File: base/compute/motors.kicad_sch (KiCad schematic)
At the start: 18 parts, among them U4 W25X20CLSN, U5 ICE40UP5K-SG48ITR-FPGA_Lattice

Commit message: compute  module ready for fab
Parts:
- U5: footprint Package_DFN_QFN:QFN-48-1EP_7x7mm_P0.5mm_EP5.6x5.6mm -> footprints:QFN-48-1EP_7x7mm_P0.5mm_EP5.6x5.6mm
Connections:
- net FPGA36 is gone; now on net SPI_SS_FPGA: U5.25 (IOT_36b)
- net FPGA37 is gone; now on net Z_PO: U5.23 (IOT_37a)
- net FPGA48 is gone; now on net DIGITAL: U5.36 (IOT_48b)
- net FPGA50 is gone; now on net HALL2: U5.38 (IOT_50b)
- net FPGA51 is gone; now on net HALL3: U5.42 (IOT_51a)
- net DIGITAL: no longer U5.31 (IOT_42b)
- net HALL1: now also U5.37 (IOT_45a_G1); no longer U5.34 (IOT_44b)
- net HALL2: no longer U5.32 (IOT_43a)
- net HALL3: no longer U5.37 (IOT_45a_G1)
- net SPI_SS_FPGA: no longer U5.10 (IOB_18a)
- net Y_DIR: now also U5.10 (IOB_18a); no longer U5.21 (IOB_23b)
- net Y_PO: now also U5.12 (IOB_22a); no longer U5.11 (IOB_20a)
- net Y_STEP: now also U5.11 (IOB_20a); no longer U5.12 (IOB_22a)
- net Z_DIR: now also U5.20 (IOB_25b_G3); no longer U5.28 (IOT_41a)
- net Z_PO: no longer U5.20 (IOB_25b_G3)
- net Z_STEP: now also U5.21 (IOB_23b); no longer U5.27 (IOT_38b)
- net +3V3 renamed +3.3V
- net FREE renamed FPGA39
- new net FPGA38: U5.27 (IOT_38b)
- new net FPGA41: U5.28 (IOT_41a)
- new net FPGA42: U5.31 (IOT_42b)
- new net FPGA43: U5.32 (IOT_43a)
- new net FPGA44: U5.34 (IOT_44b)
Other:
- note added: "SPI wires doubled, not sure on SPI on ultraplus https://github.com/YosysHQ/icestorm/issues/174"

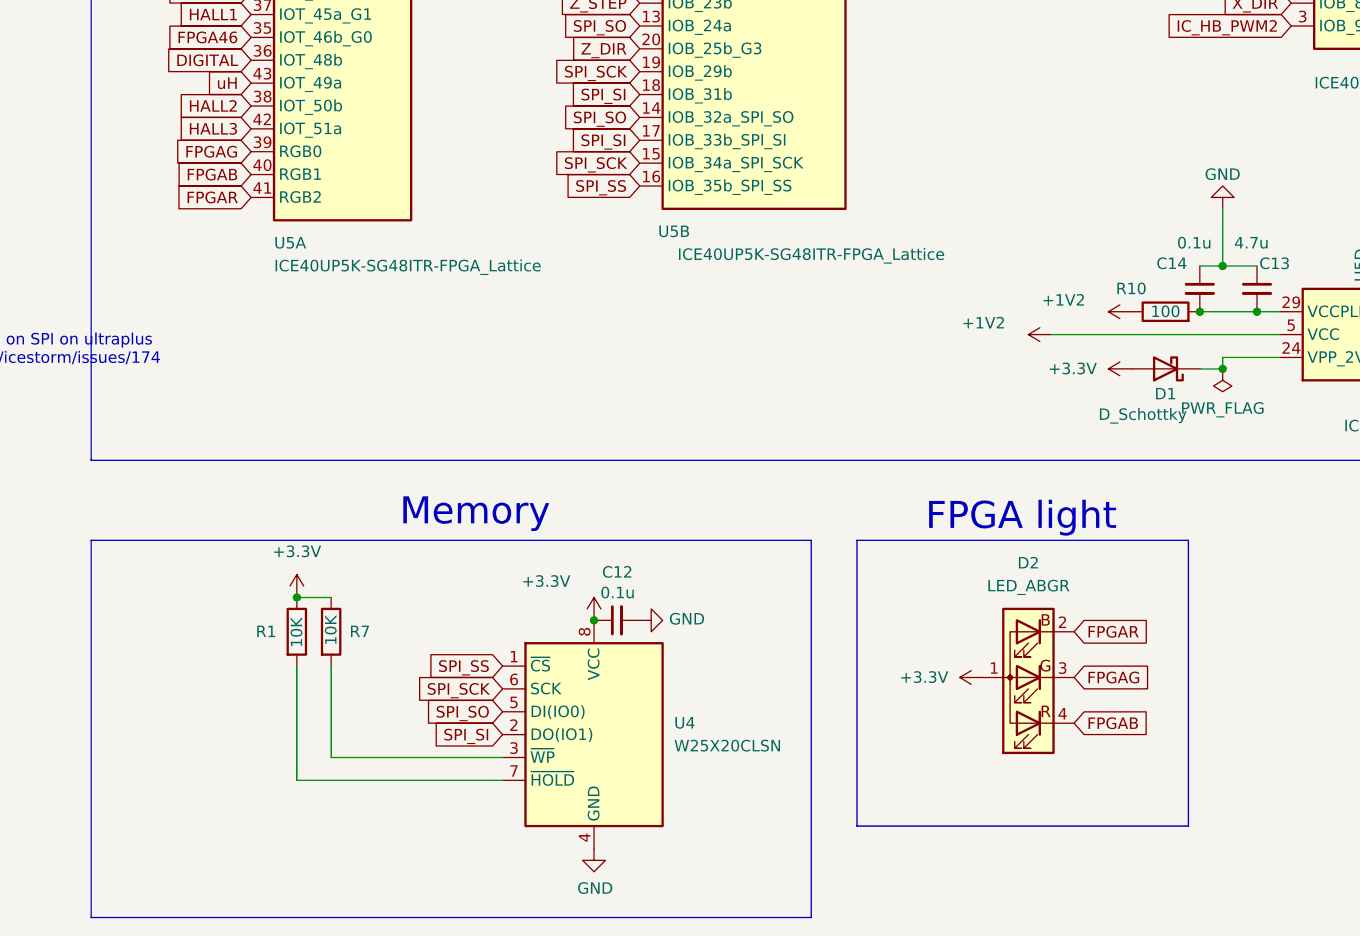
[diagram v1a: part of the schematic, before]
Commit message: moved from 2 headers to 1 smt 40 pin header
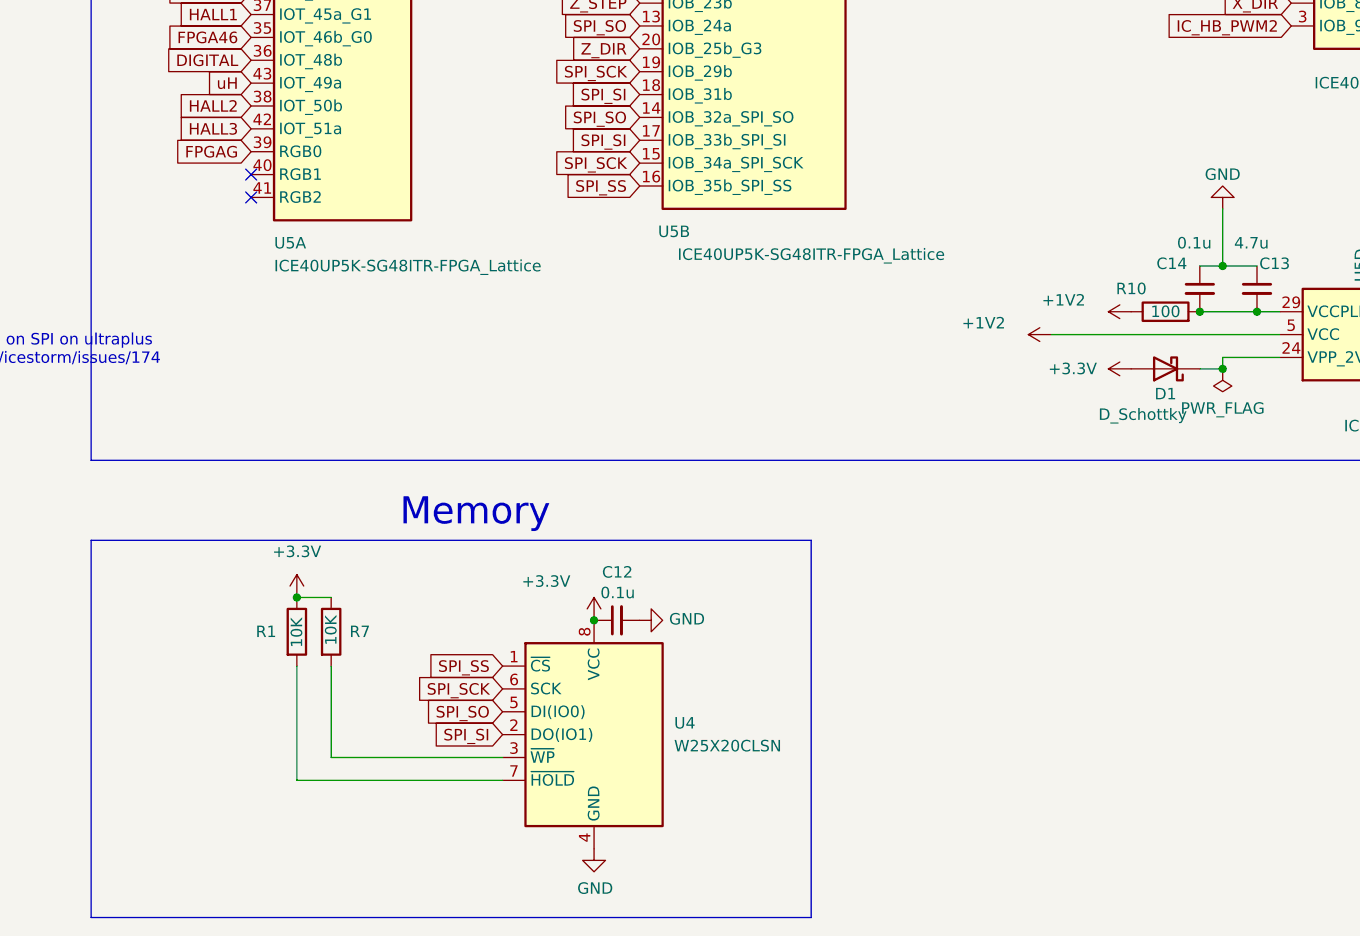
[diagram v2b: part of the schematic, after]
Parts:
- removed D2: LED_ABGR, footprints:LED_Cree-PLCC4_2x2mm_CW, symbol Device:LED_ABGR
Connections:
- net FPGAB: no longer names the net of U5.40 (RGB1)
- net FPGAR: no longer names the net of U5.41 (RGB2)
- no-connect marks 0 -> 2
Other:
- note removed: "FPGA light"

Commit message: retracking board
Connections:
- net FPGA38 is gone; now on net Z_DIR: U5.27 (IOT_38b)
- net FPGA39 is gone; now on net X_STEP: U5.26 (IOT_39a)
- net FPGA46 is gone; now on net Z_STEP: U5.35 (IOT_46b_G0)
- net DIGITAL: now also U5.46 (IOB_0a); no longer U5.36 (IOT_48b)
- net HALL1: now also U5.45 (IOB_5b); no longer U5.37 (IOT_45a_G1)
- net HALL2: now also U5.47 (IOB_2a); no longer U5.38 (IOT_50b)
- net HALL3: now also U5.48 (IOB_4a); no longer U5.42 (IOT_51a)
- net IC_HB_PWM1: now also U5.11 (IOB_20a); no longer U5.2 (IOB_6a)
- net IC_HB_PWM2: now also U5.12 (IOB_22a); no longer U5.3 (IOB_9b)
- net X_DIR: now also U5.20 (IOB_25b_G3); no longer U5.4 (IOB_8a)
- net X_PO: now also U5.42 (IOT_51a); no longer U5.9 (IOB_16a)
- net X_STEP: no longer U5.6 (IOB_13b)
- net Y_DIR: now also U5.36 (IOT_48b); no longer U5.10 (IOB_18a)
- net Y_PO: now also U5.21 (IOB_23b); no longer U5.12 (IOB_22a)
- net Y_STEP: now also U5.37 (IOT_45a_G1); no longer U5.11 (IOB_20a)
- net Z_DIR: no longer U5.20 (IOB_25b_G3)
- net Z_STEP: no longer U5.21 (IOB_23b)
- net uH: now also U5.4 (IOB_8a); no longer U5.43 (IOT_49a)
- net uL: now also U5.2 (IOB_6a); no longer U5.44 (IOB_3b_G6)
- net vH: now also U5.6 (IOB_13b); no longer U5.45 (IOB_5b)
- net vL: now also U5.3 (IOB_9b); no longer U5.46 (IOB_0a)
- net wH: now also U5.10 (IOB_18a); no longer U5.47 (IOB_2a)
- net wL: now also U5.9 (IOB_16a); no longer U5.48 (IOB_4a)
- net FPGA41 renamed INDEX_X
- new net FPGA3: U5.44 (IOB_3b_G6)
- new net FPGA49: U5.43 (IOT_49a)
- new net HALL2_old: U5.38 (IOT_50b)
